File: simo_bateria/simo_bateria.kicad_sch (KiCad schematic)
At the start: 14 parts, among them J1 BAT_LEVEL, J2 Plugin, SW1 SW_Reed, U1 mod_mt3608, U2 BSS314PEH6327XTSA1

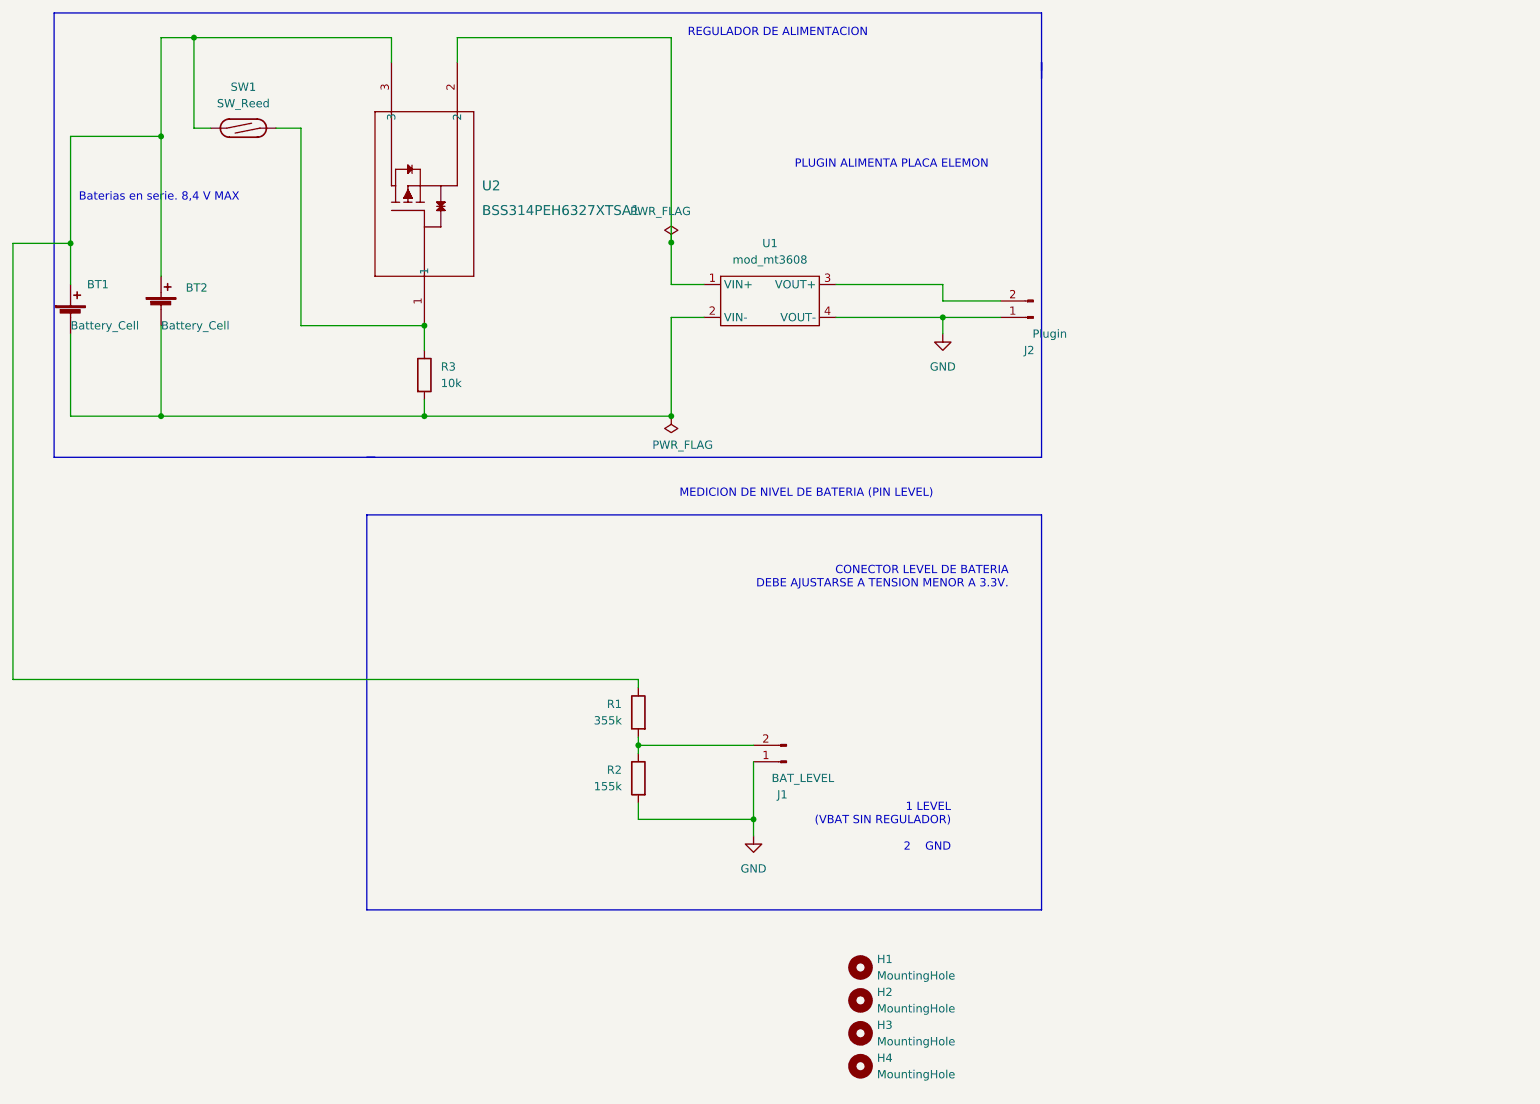
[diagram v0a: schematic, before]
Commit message: revision 3.0. Esquema. PCB con posicionamiento tentativo. Falta ver la posicion definitiva y mas conveniente del switch magnetico
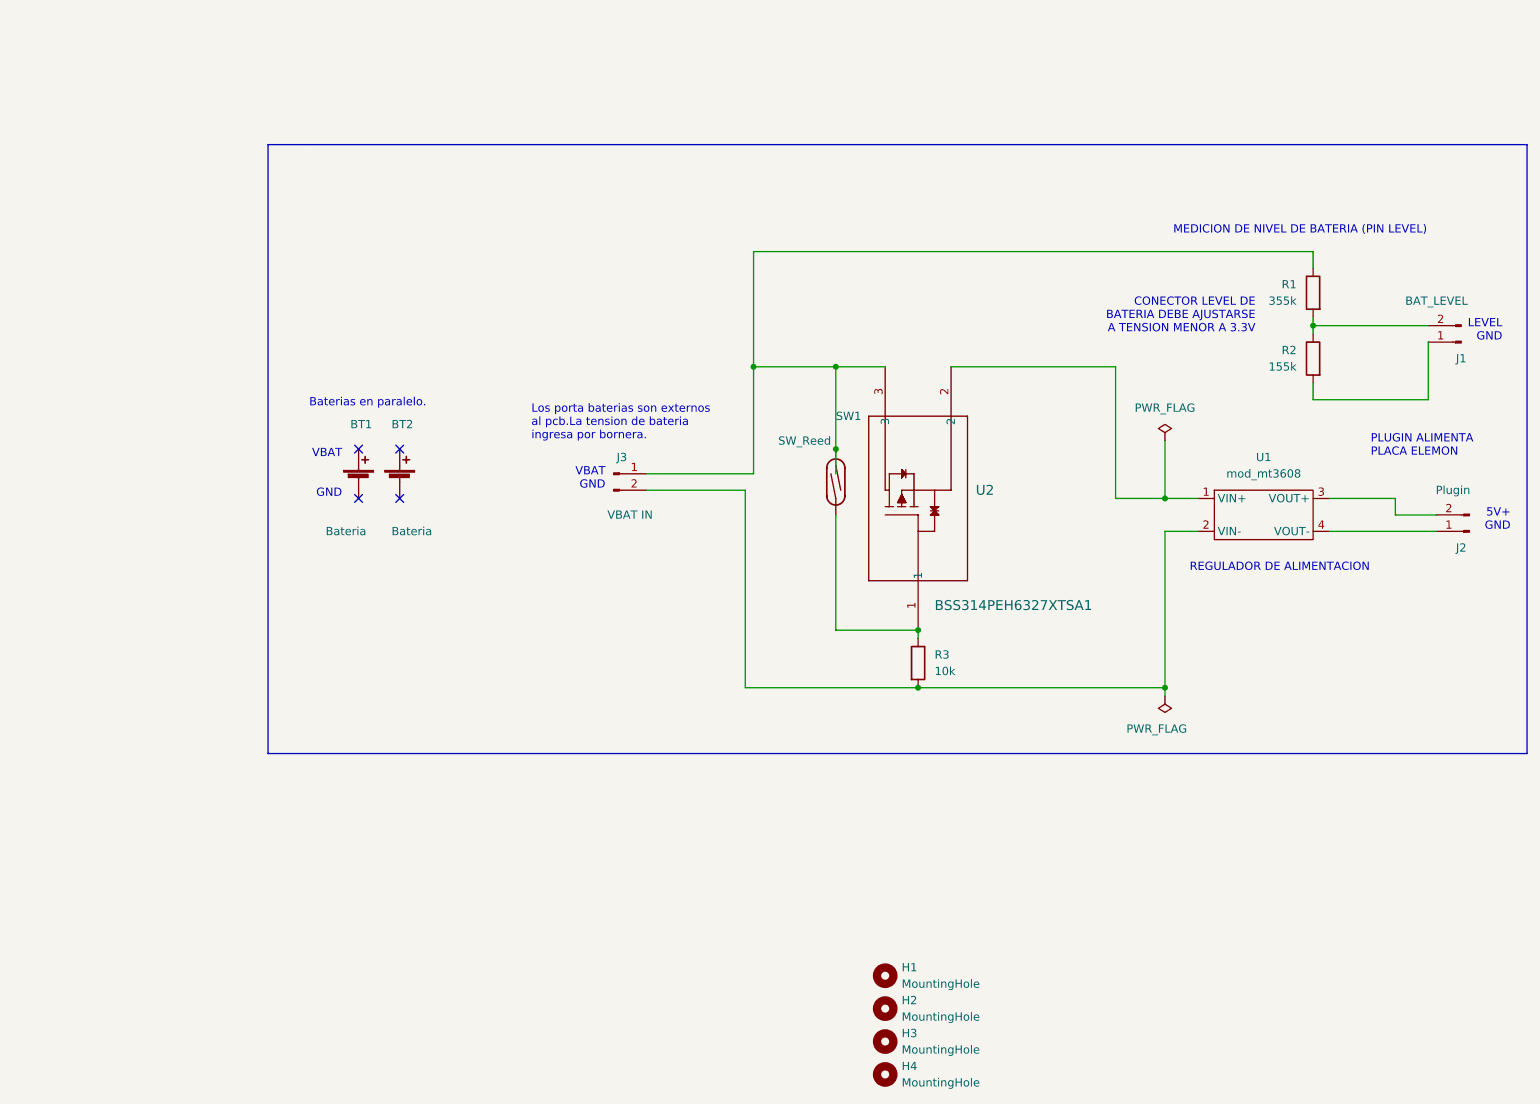
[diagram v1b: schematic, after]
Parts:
- removed U2: BSS314PEH6327XTSA1, simo_bateria:TRANS_BSS314PEH6327XTSA1_INF, symbol bss314peh627xtsa1ct-nd:BSS314PEH6327XTSA1
- added J3: VBAT IN, simo_bateria:JST_EH_B2B-EH-A_1x02_P2.50mm_Vertical, symbol simo_bateria:Conn_01x02_Male
- added U2: BSS314PEH6327XTSA1, simo_bateria:TRANS_BSS314PEH6327XTSA1_INF, symbol simo_bateria:BSS314PEH6327XTSA1
- BT1, BT2: value Battery_Cell -> Bateria; footprint simo_bateria:BatteryHolder_MPD_BH-18650-PC2 -> simo_bateria:BH-18650-PC2_virtual; Bateria https://www.efestpower.com/index.php?ac=article&at=read&did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 -> https://www.efestargentina.com.ar/18650.php
- R1, R2, R3, SW1: footprint Resistor_THT:R_Axial_DIN0309_L9.0mm_D3.2mm_P25.40mm_Horizontal -> Resistor_THT:R_Axial_DIN0309_L9.0mm_D3.2mm_P15.24mm_Horizontal
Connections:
- net at R1.1, SW1.1: now also J3.1 (Pin_1), U2.3; no longer BT1.1 (+), BT2.1 (+)
- net at R3.2, U1.2 (VIN-): now also J3.2 (Pin_2); no longer BT1.2 (-), BT2.2 (-)
- net at R3.1, SW1.2: now also U2.1
- net at U1.1 (VIN+): now also U2.2
- net GND: no longer names the net of J1.1 (Pin_1), R2.2
- net GND: no longer J2.1 (Pin_1), U1.4 (VOUT-)
- new net: J2.1 (Pin_1), U1.4 (VOUT-)
- no-connect marks 0 -> 4
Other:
- note added: "5V+ GND"
- note added: "Baterias en paralelo."
- note added: "CONECTOR LEVEL DE BATERIA DEBE AJUSTARSE A TENSION MENOR A 3.3V"
- note added: "LEVEL GND"
- note added: "Los porta baterias son externos al pcb.La tension de bateria ingresa por bornera."
- note added: "VBAT GND"
- note removed: "1 LEVEL (VBAT SIN REGULADOR) 2 GND"
- note removed: "Baterias en serie. 8,4 V MAX"
- note removed: "CONECTOR LEVEL DE BATERIA DEBE AJUSTARSE A TENSION MENOR A 3.3V."
- moved on the sheet: BT1, BT2, J1, J2, R1, R2, R3, SW1

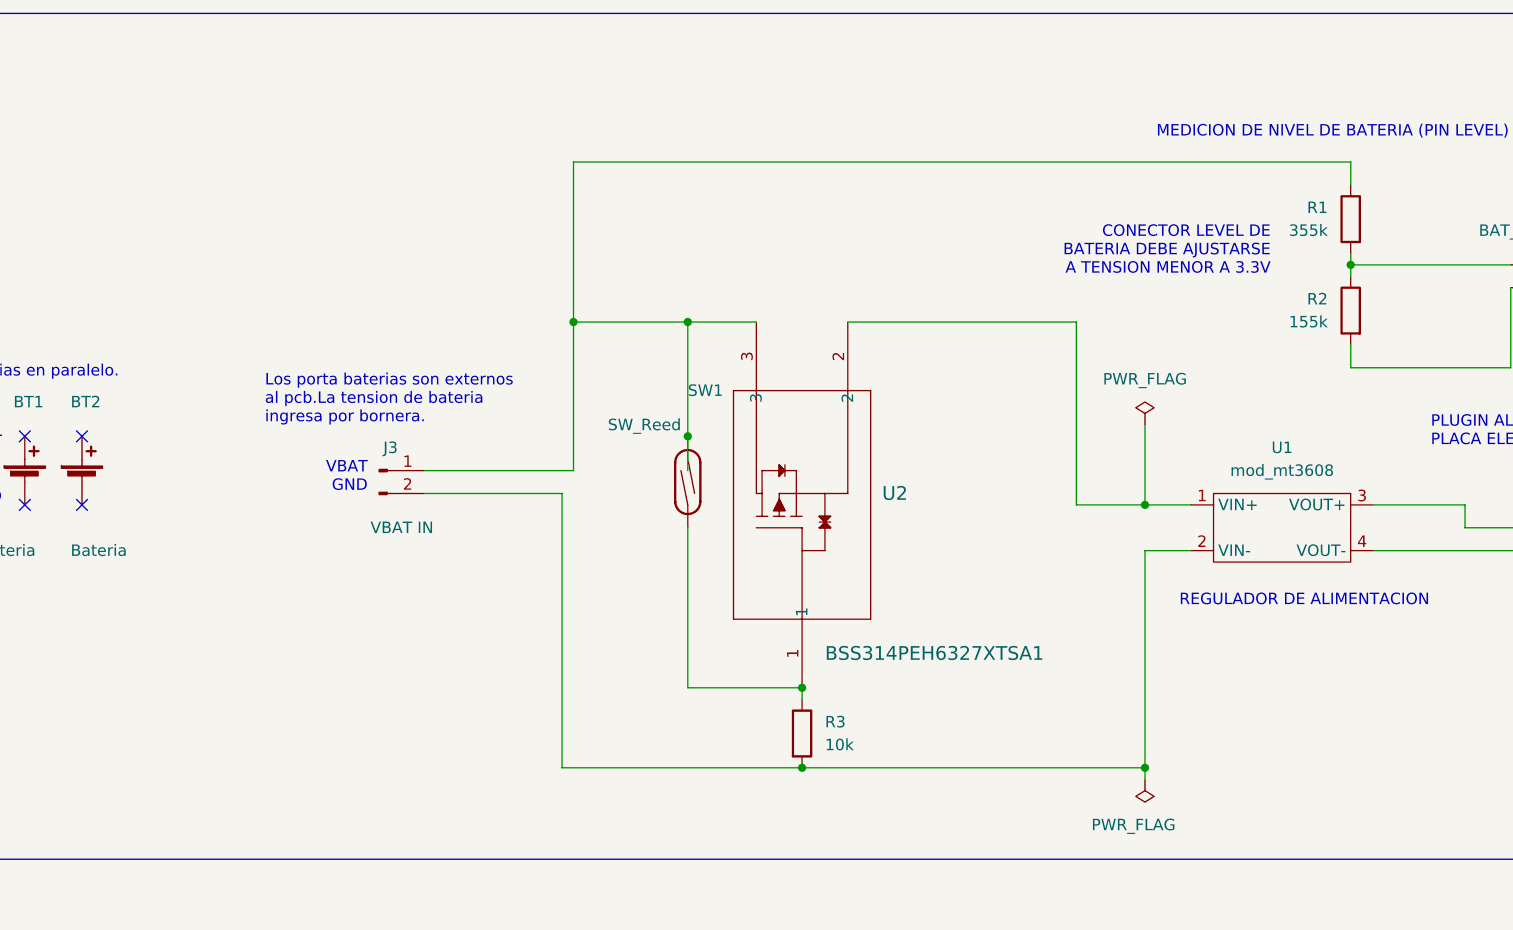
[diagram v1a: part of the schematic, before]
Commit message: se agrego bornera para el switch magnetico. El pcb tengo 2 warnings a revisar
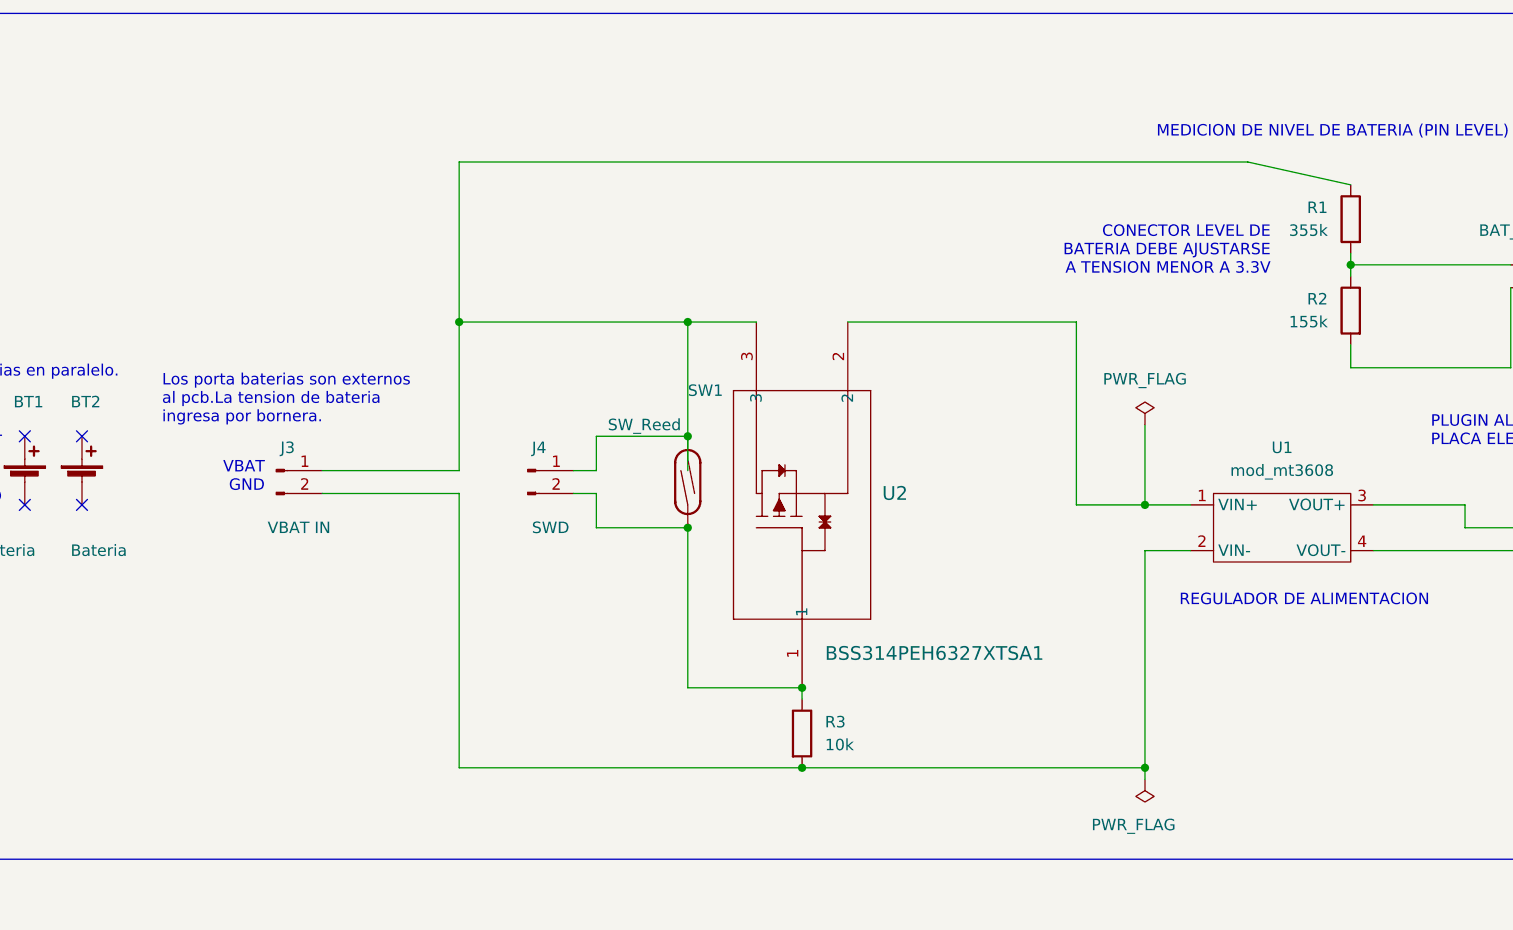
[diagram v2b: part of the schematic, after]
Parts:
- added J4: SWD, simo_bateria:JST_EH_B2B-EH-A_1x02_P2.50mm_Vertical, symbol simo_bateria:Conn_01x02_Male
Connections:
- net at R3.1, SW1.2, U2.1: now also J4.2 (Pin_2)
- net at J3.1 (Pin_1), R1.1, SW1.1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: now also J4.1 (Pin_1)
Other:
- moved on the sheet: J3
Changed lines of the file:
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@@
     (comment 4 "Placa de conexion para elementos de la bateria.")
   )
+  (junction (at 115.57 77.47) (diameter 0) (color 0 0 0 0)
+  )
   (junction (at 191.77 97.79) (diameter 0) (color 0 0 0 0)
   )
@@
   (junction (at 191.77 127) (diameter 0) (color 0 0 0 0)
   )
+  (junction (at 140.97 100.33) (diameter 0) (color 0 0 0 0)
+  )
   (junction (at 140.97 77.47) (diameter 0) (color 0 0 0 0)
   )
@@
   )
   (junction (at 153.67 127) (diameter 0) (color 0 0 0 0)
-  )
-  (junction (at 128.27 77.47) (diameter 0) (color 0 0 0 0)
   )
   (no_connect (at 67.31 97.79))
@@
     (stroke (width 0) (type default) (color 0 0 0 0))
   )
-  (wire (pts (xy 128.27 59.69) (xy 128.27 77.47))
+  (wire (pts (xy 115.57 59.69) (xy 115.57 77.47))
     (stroke (width 0) (type default) (color 0 0 0 0))
   )
@@
     (stroke (width 0) (type default) (color 0 0 0 0))
   )
-  (wire (pts (xy 111.76 96.52) (xy 127 96.52))
+  (wire (pts (xy 115.57 77.47) (xy 140.97 77.47))
+    (stroke (width 0) (type default) (color 0 0 0 0))
+  )
+  (wire (pts (xy 100.33 96.52) (xy 115.57 96.52))
     (stroke (width 0) (type default) (color 0 0 0 0))
   )
@@
     (stroke (width 0) (type default) (color 0 0 0 0))
   )
-  (wire (pts (xy 111.76 93.98) (xy 128.27 93.98))
-    (stroke (width 0) (type default) (color 0 0 0 0))
-  )
-  (wire (pts (xy 128.27 59.69) (xy 214.63 59.69))
-    (stroke (width 0) (type default) (color 0 0 0 0))
-  )
-  (wire (pts (xy 214.63 59.69) (xy 214.63 62.23))
+  (wire (pts (xy 130.81 90.17) (xy 140.97 90.17))
+    (stroke (width 0) (type default) (color 0 0 0 0))
+  )
+  (wire (pts (xy 100.33 93.98) (xy 115.57 93.98))
+    (stroke (width 0) (type default) (color 0 0 0 0))
+  )
+  (wire (pts (xy 115.57 59.69) (xy 203.2 59.69))
+    (stroke (width 0) (type default) (color 0 0 0 0))
+  )
+  (wire (pts (xy 203.2 59.69) (xy 214.63 62.23))
     (stroke (width 0) (type default) (color 0 0 0 0))
   )
@@
     (stroke (width 0) (type default) (color 0 0 0 0))
   )
+  (wire (pts (xy 130.81 93.98) (xy 130.81 90.17))
+    (stroke (width 0) (type default) (color 0 0 0 0))
+  )
   (polyline (pts (xy 53.34 43.18) (xy 59.69 43.18))
     (stroke (width 0) (type default) (color 0 0 0 0))
   )
-  (wire (pts (xy 128.27 77.47) (xy 128.27 93.98))
+  (wire (pts (xy 115.57 77.47) (xy 115.57 93.98))
     (stroke (width 0) (type default) (color 0 0 0 0))
   )
@@
     (stroke (width 0) (type default) (color 0 0 0 0))
   )
-  (wire (pts (xy 127 96.52) (xy 127 127))
+  (wire (pts (xy 115.57 96.52) (xy 115.57 127))
     (stroke (width 0) (type default) (color 0 0 0 0))
   )
@@
     (stroke (width 0) (type default) (color 0 0 0 0))
   )
+  (wire (pts (xy 128.27 96.52) (xy 130.81 96.52))
+    (stroke (width 0) (type default) (color 0 0 0 0))
+  )
   (wire (pts (xy 140.97 118.11) (xy 153.67 118.11))
     (stroke (width 0) (type default) (color 0 0 0 0))
@@
     (stroke (width 0) (type default) (color 0 0 0 0))
   )
+  (wire (pts (xy 130.81 96.52) (xy 130.81 100.33))
+    (stroke (width 0) (type default) (color 0 0 0 0))
+  )
   (wire (pts (xy 232.41 82.55) (xy 214.63 82.55))
     (stroke (width 0) (type default) (color 0 0 0 0))
   )
+  (wire (pts (xy 130.81 100.33) (xy 140.97 100.33))
+    (stroke (width 0) (type default) (color 0 0 0 0))
+  )
   (wire (pts (xy 232.41 73.66) (xy 232.41 82.55))
     (stroke (width 0) (type default) (color 0 0 0 0))
   )
-  (wire (pts (xy 128.27 77.47) (xy 140.97 77.47))
-    (stroke (width 0) (type default) (color 0 0 0 0))
-  )
-  (wire (pts (xy 127 127) (xy 153.67 127))
+  (wire (pts (xy 115.57 127) (xy 153.67 127))
+    (stroke (width 0) (type default) (color 0 0 0 0))
+  )
+  (wire (pts (xy 128.27 93.98) (xy 130.81 93.98))
     (stroke (width 0) (type default) (color 0 0 0 0))
   )
@@
   )
   (text "Los porta baterias son externos\nal pcb.La tension de bateria \ningresa por bornera."
-    (at 93.98 88.9 0)
+    (at 82.55 88.9 0)
     (effects (font (size 1.27 1.27)) (justify left bottom))
   )
@@
     (effects (font (size 1.27 1.27)) (justify right bottom))
   )
-  (text "VBAT\nGND\n" (at 105.41 96.52 180)
+  (text "VBAT\nGND\n" (at 93.98 96.52 180)
     (effects (font (size 1.27 1.27)) (justify right bottom))
   )
@@
     )
   )
+  (symbol (lib_id "simo_bateria:Conn_01x02_Male") (at 123.19 93.98 0) (unit 1)
+    (in_bom yes) (on_board yes)
+    (property "Reference" "J4" (id 0) (at 124.46 91.44 0))
+    (property "Value" "SWD" (id 1) (at 125.73 100.33 0))
+    (property "Footprint" "simo_bateria:JST_EH_B2B-EH-A_1x02_P2.50mm_Vertical" (id 2) (at 123.19 93.98 0)
+      (effects (font (size 1.27 1.27)) hide)
+    )
+    (property "Datasheet" "https://www.jst-mfg.com/product/pdf/eng/eEH.pdf" (id 3) (at 123.19 93.98 0)
+      (effects (font (size 1.27 1.27)) hide)
+    )
+    (property "Digikey" "455-1611-ND" (id 4) (at 123.19 93.98 0)
+      (effects (font (size 1.27 1.27)) hide)
+    )
+    (property "Codigo" "B2B-EH-A(LF)(SN)" (id 5) (at 123.19 93.98 0)
+      (effects (font (size 1.27 1.27)) hide)
+    )
+    (pin "1")
+    (pin "2")
+  )
   (symbol (lib_id "Device:Battery_Cell") (at 73.66 95.25 0) (unit 1)
     (in_bom yes) (on_board yes)
@@
     (pin "2")
   )
-  (symbol (lib_id "simo_bateria:Conn_01x02_Male") (at 106.68 93.98 0) (unit 1)
-    (in_bom yes) (on_board yes)
-    (property "Reference" "J3" (id 0) (at 107.95 91.44 0))
-    (property "Value" "VBAT IN" (id 1) (at 109.22 100.33 0))
-    (property "Footprint" "simo_bateria:JST_EH_B2B-EH-A_1x02_P2.50mm_Vertical" (id 2) (at 106.68 93.98 0)
-      (effects (font (size 1.27 1.27)) hide)
-    )
-    (property "Datasheet" "https://www.jst-mfg.com/product/pdf/eng/eEH.pdf" (id 3) (at 106.68 93.98 0)
-      (effects (font (size 1.27 1.27)) hide)
-    )
-    (property "Digikey" "455-1611-ND" (id 4) (at 106.68 93.98 0)
-      (effects (font (size 1.27 1.27)) hide)
-    )
-    (property "Codigo" "B2B-EH-A(LF)(SN)" (id 5) (at 106.68 93.98 0)
+  (symbol (lib_id "simo_bateria:Conn_01x02_Male") (at 95.25 93.98 0) (unit 1)
+    (in_bom yes) (on_board yes)
+    (property "Reference" "J3" (id 0) (at 96.52 91.44 0))
+    (property "Value" "VBAT IN" (id 1) (at 97.79 100.33 0))
+    (property "Footprint" "simo_bateria:JST_EH_B2B-EH-A_1x02_P2.50mm_Vertical" (id 2) (at 95.25 93.98 0)
+      (effects (font (size 1.27 1.27)) hide)
+    )
+    (property "Datasheet" "https://www.jst-mfg.com/product/pdf/eng/eEH.pdf" (id 3) (at 95.25 93.98 0)
+      (effects (font (size 1.27 1.27)) hide)
+    )
+    (property "Digikey" "455-1611-ND" (id 4) (at 95.25 93.98 0)
+      (effects (font (size 1.27 1.27)) hide)
+    )
+    (property "Codigo" "B2B-EH-A(LF)(SN)" (id 5) (at 95.25 93.98 0)
       (effects (font (size 1.27 1.27)) hide)
     )
@@
       (reference "J3") (unit 1) (value "VBAT IN") (footprint "simo_bateria:JST_EH_B2B-EH-A_1x02_P2.50mm_Vertical")
     )
+    (path "/4a7c6fca-8415-4e2d-a55a-6ce644bd85e5"
+      (reference "J4") (unit 1) (value "SWD") (footprint "simo_bateria:JST_EH_B2B-EH-A_1x02_P2.50mm_Vertical")
+    )
     (path "/8da78f3b-5575-47f1-9326-e93636a9e26c"

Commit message: Update
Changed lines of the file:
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@@
+    (stroke (width 0) (type default) (color 0 0 0 0))
+  )
+  (wire (pts (xy 214.63 59.69) (xy 214.63 62.23))
     (stroke (width 0) (type default) (color 0 0 0 0))
   )
@@
     (stroke (width 0) (type default) (color 0 0 0 0))
   )
-  (wire (pts (xy 115.57 59.69) (xy 203.2 59.69))
+  (wire (pts (xy 115.57 59.69) (xy 214.63 59.69))
     (stroke (width 0) (type default) (color 0 0 0 0))
   )
-  (wire (pts (xy 203.2 59.69) (xy 214.63 62.23))
-    (stroke (width 0) (type default) (color 0 0 0 0))
-  )
